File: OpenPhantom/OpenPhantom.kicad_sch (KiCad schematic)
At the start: 105 parts, among them J1 Barrel_Jack, J2 Video, J3 Audio, Q1 BC548, Q2 BD136, Q3 BC557, Q4 BC548, SW1 POWER, SW2 RESET, U1 UM6116 VRAM, U10 74HC368, U11 74HC368, U2 UM6116 WRAM, U3 74HC04, U4 UA6547_CPU, U5 4013, U6 UA6548_PPU, U7 74HC139, U8 74LS373, U9 LM7805_TO220, Y1 21.453366 MHz

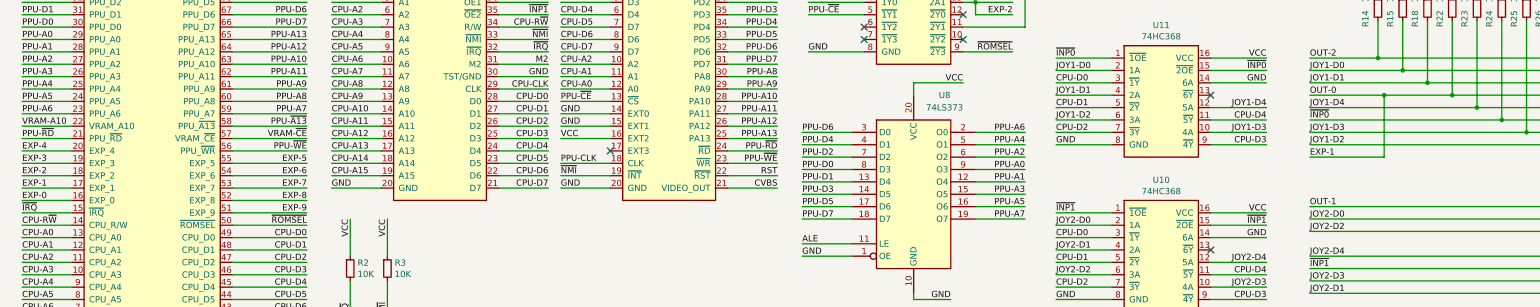
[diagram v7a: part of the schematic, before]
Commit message: Joy port fix.
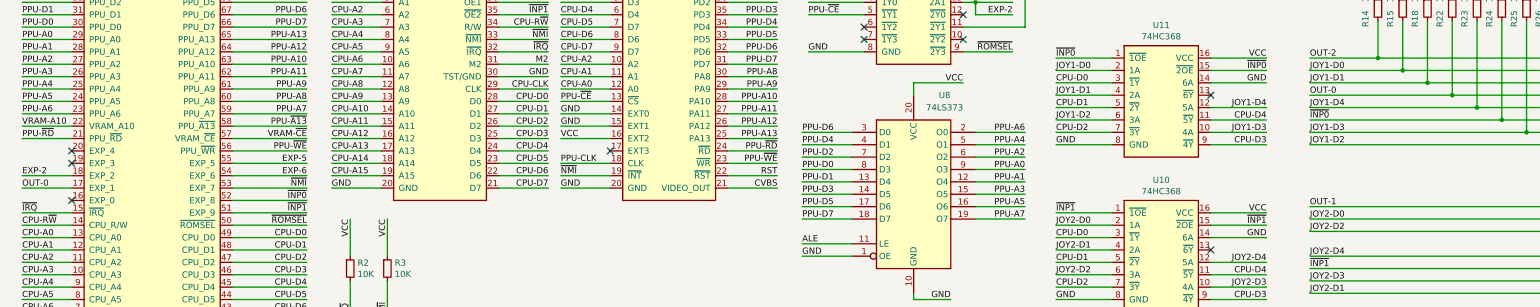
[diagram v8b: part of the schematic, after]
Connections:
- net EXP-7 is gone; now on net ~{NMI}: SLOT1.53 (EXP_7)
- net EXP-8 is gone; now on net ~{INP0}: SLOT1.52 (EXP_8)
- net EXP-9 is gone; now on net ~{INP1}: SLOT1.51 (EXP_9)
- net EXP-0: no longer names the net of SLOT1.16 (EXP_0)
- net EXP-1 renamed OUT-0
- net EXP-3: no longer names the net of SLOT1.19 (EXP_3)
- net EXP-4: no longer names the net of SLOT1.20 (EXP_4)
- no-connect marks 12 -> 15
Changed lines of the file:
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@@
   (junction (at 375.92 130.81) (diameter 0) (color 0 0 0 0)
   )
-  (junction (at 297.18 52.07) (diameter 0) (color 0 0 0 0)
-  )
   (junction (at 351.79 26.67) (diameter 0) (color 0 0 0 0)
   )
@@
   )
   (no_connect (at 190.5 40.64))
+  (no_connect (at 27.94 63.5))
   (no_connect (at 261.62 52.07))
   (no_connect (at 60.96 27.94))
@@
   (no_connect (at 120.65 133.35))
   (no_connect (at 27.94 25.4))
+  (no_connect (at 27.94 73.66))
+  (no_connect (at 27.94 66.04))
   (no_connect (at 210.82 35.56))
   (no_connect (at 27.94 27.94))
@@
     (stroke (width 0) (type default) (color 0 0 0 0))
   )
-  (wire (pts (xy 297.18 64.77) (xy 297.18 52.07))
-    (stroke (width 0) (type default) (color 0 0 0 0))
-  )
   (wire (pts (xy 367.03 201.93) (xy 369.57 201.93))
     (stroke (width 0) (type default) (color 0 0 0 0))
@@
     (stroke (width 0) (type default) (color 0 0 0 0))
   )
-  (wire (pts (xy 281.94 52.07) (xy 297.18 52.07))
-    (stroke (width 0) (type default) (color 0 0 0 0))
-  )
   (wire (pts (xy 27.94 106.68) (xy 17.78 106.68))
     (stroke (width 0) (type default) (color 0 0 0 0))
@@
     (stroke (width 0) (type default) (color 0 0 0 0))
   )
-  (wire (pts (xy 281.94 64.77) (xy 297.18 64.77))
-    (stroke (width 0) (type default) (color 0 0 0 0))
-  )
   (wire (pts (xy 162.56 35.56) (xy 172.72 35.56))
     (stroke (width 0) (type default) (color 0 0 0 0))
@@
     (stroke (width 0) (type default) (color 0 0 0 0))
   )
-  (wire (pts (xy 27.94 73.66) (xy 17.78 73.66))
-    (stroke (width 0) (type default) (color 0 0 0 0))
-  )
   (wire (pts (xy 166.37 245.11) (xy 166.37 241.3))
     (stroke (width 0) (type default) (color 0 0 0 0))
@@
     (stroke (width 0) (type default) (color 0 0 0 0))
   )
-  (wire (pts (xy 27.94 66.04) (xy 17.78 66.04))
-    (stroke (width 0) (type default) (color 0 0 0 0))
-  )
   (wire (pts (xy 331.47 26.67) (xy 336.55 26.67))
     (stroke (width 0) (type default) (color 0 0 0 0))
@@
     (stroke (width 0) (type default) (color 0 0 0 0))
   )
-  (wire (pts (xy 297.18 52.07) (xy 311.15 52.07))
+  (wire (pts (xy 281.94 52.07) (xy 311.15 52.07))
     (stroke (width 0) (type default) (color 0 0 0 0))
   )
@@
   )
   (wire (pts (xy 138.43 55.88) (xy 128.27 55.88))
-    (stroke (width 0) (type default) (color 0 0 0 0))
-  )
-  (wire (pts (xy 27.94 63.5) (xy 17.78 63.5))
     (stroke (width 0) (type default) (color 0 0 0 0))
   )
@@
     (effects (font (size 1.27 1.27)) (justify right bottom))
   )
-  (label "EXP-4" (at 17.78 63.5 0)
-    (effects (font (size 1.27 1.27)) (justify left bottom))
-  )
   (label "PPU-D1" (at 177.8 69.85 0)
     (effects (font (size 1.27 1.27)) (justify left bottom))
@@
     (effects (font (size 1.27 1.27)) (justify right bottom))
   )
-  (label "EXP-0" (at 17.78 73.66 0)
-    (effects (font (size 1.27 1.27)) (justify left bottom))
-  )
   (label "CPU-D3" (at 128.27 33.02 0)
     (effects (font (size 1.27 1.27)) (justify left bottom))
@@
     (effects (font (size 1.27 1.27)) (justify left bottom))
   )
-  (label "EXP-1" (at 281.94 64.77 0)
-    (effects (font (size 1.27 1.27)) (justify left bottom))
-  )
   (label "GND" (at 170.18 173.99 90)
     (effects (font (size 1.27 1.27)) (justify left bottom))
@@
     (effects (font (size 1.27 1.27)) (justify right bottom))
   )
-  (label "EXP-9" (at 76.2 76.2 180)
+  (label "~{INP1}" (at 76.2 76.2 180)
     (effects (font (size 1.27 1.27)) (justify right bottom))
   )
@@
     (effects (font (size 1.27 1.27)) (justify left bottom))
   )
-  (label "EXP-8" (at 76.2 73.66 180)
+  (label "~{INP0}" (at 76.2 73.66 180)
     (effects (font (size 1.27 1.27)) (justify right bottom))
   )
@@
     (effects (font (size 1.27 1.27)) (justify right bottom))
   )
-  (label "EXP-3" (at 17.78 66.04 0)
-    (effects (font (size 1.27 1.27)) (justify left bottom))
-  )
   (label "CVBS" (at 307.34 223.52 0)
     (effects (font (size 1.27 1.27)) (justify left bottom))
@@
     (effects (font (size 1.27 1.27)) (justify left bottom))
   )
-  (label "EXP-7" (at 76.2 71.12 180)
+  (label "~{NMI}" (at 76.2 71.12 180)
     (effects (font (size 1.27 1.27)) (justify right bottom))
   )
@@
     (effects (font (size 1.27 1.27)) (justify left bottom))
   )
-  (label "EXP-1" (at 17.78 71.12 0)
-    (effects (font (size 1.27 1.27)) (justify left bottom))
-  )
+  (label "OUT-0" (at 17.78 71.12 0)
+    (effects (font (size 1.27 1.27)) (justify left bottom))
+  )
